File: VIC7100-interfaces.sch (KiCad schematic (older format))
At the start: 56 parts, among them Q5 DMG1012UW, U13 VIC7100

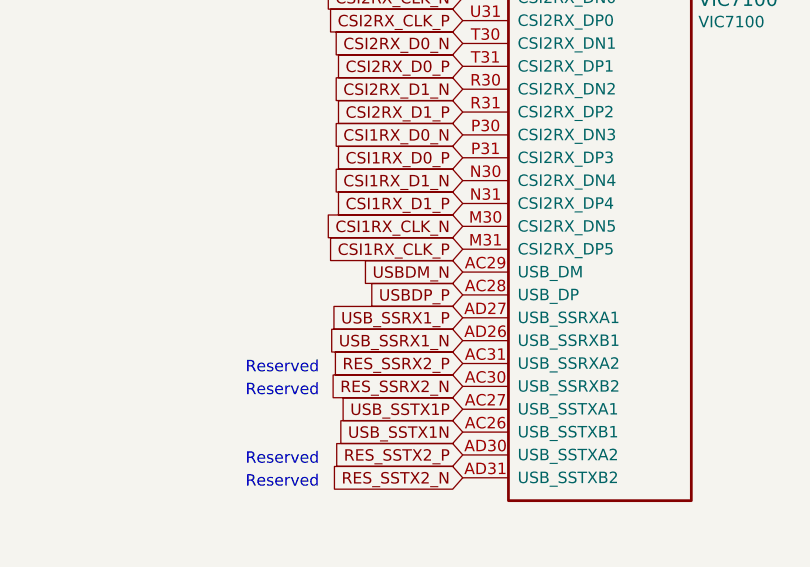
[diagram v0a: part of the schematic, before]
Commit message: Routed USB, QSPI, JTAG
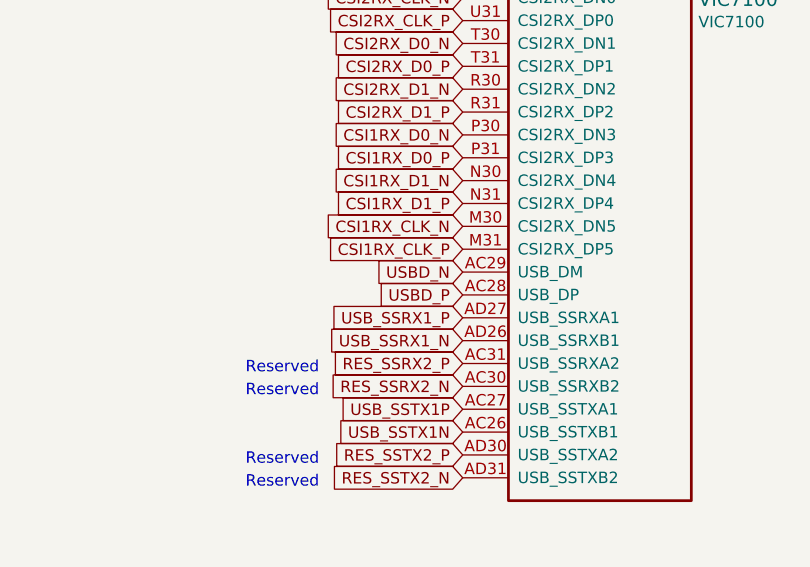
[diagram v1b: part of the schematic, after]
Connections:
- net USBDM_N renamed USBD_N
- net USBDP_P renamed USBD_P
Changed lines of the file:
@@
 CSI1RX_CLK_P
 Text GLabel 8975 4650 0    50   Input ~ 0
-USBDM_N
+USBD_N
 Text GLabel 8975 4750 0    50   Input ~ 0
-USBDP_P
+USBD_P
 Text GLabel 11925 2525 1    50   Input ~ 0
 VCC_3V3

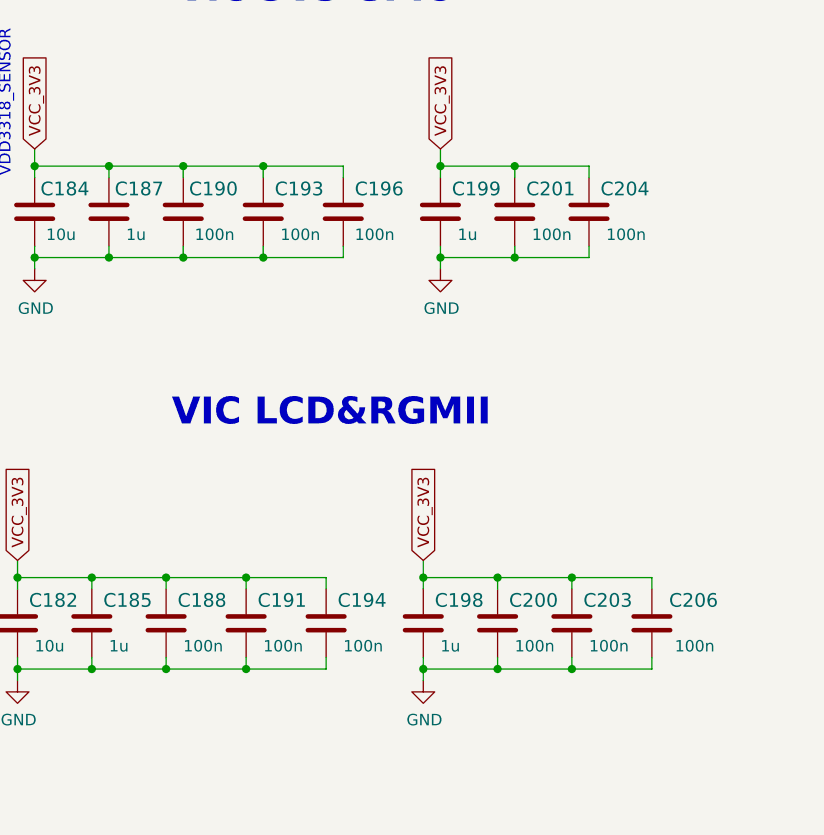
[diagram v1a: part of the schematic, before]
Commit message: Caps cleared, module connnetors' GND optimized
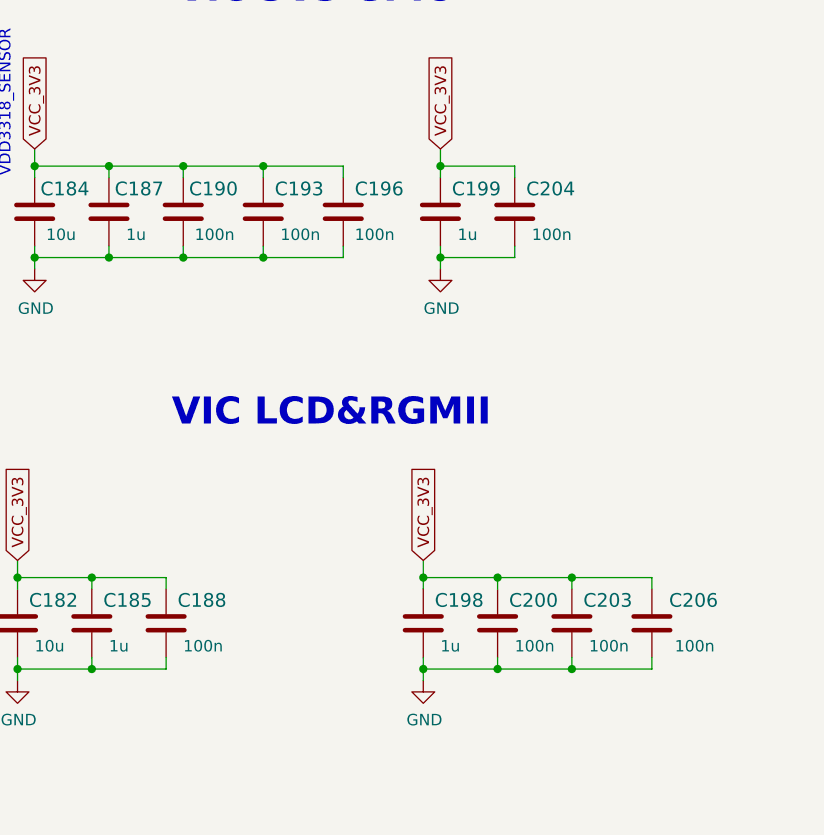
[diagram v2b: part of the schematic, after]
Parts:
- removed C191, C194, C201: C_100n_0201, arvsom-footprints:0201-res, symbol arvsom:C_100n_0201
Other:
- moved on the sheet: C204
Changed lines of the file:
@@
 Wire Wire Line
 	14025 2650 14025 2600
-Connection ~ 14025 2600
-Wire Wire Line
-	14025 2600 14350 2600
-Wire Wire Line
-	14350 2650 14350 2600
 Wire Wire Line
 	14025 2950 14025 3000
-Connection ~ 14025 3000
-Wire Wire Line
-	14025 3000 14350 3000
-Wire Wire Line
-	14350 2950 14350 3000
 $Comp
 L arvsom:C_1u_0402 C?
@@
 $Comp
 L arvsom:C_100n_0201 C?
-U 1 1 60E65122
+U 1 1 60E6512B
 P 14025 2800
-AR Path="/607683D6/60E65122" Ref="C?"  Part="1"
-AR Path="/60805CEC/60E65122" Ref="C201"  Part="1"
-F 0 "C201" H 14075 2900 60  0000 L CNN
+AR Path="/607683D6/60E6512B" Ref="C?"  Part="1"
+AR Path="/60805CEC/60E6512B" Ref="C204"  Part="1"
+F 0 "C204" H 14075 2900 60  0000 L CNN
 F 1 "C_100n_0201" H 14025 2650 60  0001 C CNN
 F 2 "arvsom-footprints:0201-res" H 14225 3000 60  0001 L CNN
@@
 F 6 "100n" H 14100 2700 50  0000 L CNN "Val"
 	1    14025 2800
-	1    0    0    -1
-$EndComp
-$Comp
-L arvsom:C_100n_0201 C?
-U 1 1 60E6512B
-P 14350 2800
-AR Path="/607683D6/60E6512B" Ref="C?"  Part="1"
-AR Path="/60805CEC/60E6512B" Ref="C204"  Part="1"
-F 0 "C204" H 14400 2900 60  0000 L CNN
-F 1 "C_100n_0201" H 14350 2650 60  0001 C CNN
-F 2 "arvsom-footprints:0201-res" H 14550 3000 60  0001 L CNN
-F 3 "" H 14350 2800 50  0001 C CNN
-F 4 "YAGEO" H 14550 3200 60  0001 L CNN "Manufacturer"
-F 5 "CC0201KRX6S5BB104" H 14550 3100 60  0001 L CNN "MPN"
-F 6 "100n" H 14425 2700 50  0000 L CNN "Val"
-	1    14350 2800
 	1    0    0    -1
 $EndComp
@@
 Wire Wire Line
 	12500 4450 12500 4400
-Connection ~ 12500 4400
 Wire Wire Line
 	12175 4750 12175 4800
@@
 Wire Wire Line
 	12500 4750 12500 4800
-Connection ~ 12500 4800
 $Comp
 L arvsom:C_10u_0402 C?
@@
 	1    0    0    -1
 $EndComp
-$Comp
-L arvsom:C_100n_0201 C?
-U 1 1 60E65169
-P 12850 4600
-AR Path="/607683D6/60E65169" Ref="C?"  Part="1"
-AR Path="/60805CEC/60E65169" Ref="C191"  Part="1"
-F 0 "C191" H 12900 4700 60  0000 L CNN
-F 1 "C_100n_0201" H 12850 4450 60  0001 C CNN
-F 2 "arvsom-footprints:0201-res" H 13050 4800 60  0001 L CNN
-F 3 "" H 12850 4600 50  0001 C CNN
-F 4 "YAGEO" H 13050 5000 60  0001 L CNN "Manufacturer"
-F 5 "CC0201KRX6S5BB104" H 13050 4900 60  0001 L CNN "MPN"
-F 6 "100n" H 12925 4500 50  0000 L CNN "Val"
-	1    12850 4600
-	1    0    0    -1
-$EndComp
-Wire Wire Line
-	13200 4750 13200 4800
-Wire Wire Line
-	13200 4450 13200 4400
-$Comp
-L arvsom:C_100n_0201 C?
-U 1 1 60E65174
-P 13200 4600
-AR Path="/607683D6/60E65174" Ref="C?"  Part="1"
-AR Path="/60805CEC/60E65174" Ref="C194"  Part="1"
-F 0 "C194" H 13250 4700 60  0000 L CNN
-F 1 "C_100n_0201" H 13200 4450 60  0001 C CNN
-F 2 "arvsom-footprints:0201-res" H 13400 4800 60  0001 L CNN
-F 3 "" H 13200 4600 50  0001 C CNN
-F 4 "YAGEO" H 13400 5000 60  0001 L CNN "Manufacturer"
-F 5 "CC0201KRX6S5BB104" H 13400 4900 60  0001 L CNN "MPN"
-F 6 "100n" H 13275 4500 50  0000 L CNN "Val"
-	1    13200 4600
-	1    0    0    -1
-$EndComp
-Wire Wire Line
-	12500 4400 12850 4400
-Wire Wire Line
-	12500 4800 12850 4800
-Wire Wire Line
-	12850 4450 12850 4400
-Connection ~ 12850 4400
-Wire Wire Line
-	12850 4400 13200 4400
-Wire Wire Line
-	12850 4750 12850 4800
-Connection ~ 12850 4800
-Wire Wire Line
-	12850 4800 13200 4800
 Text GLabel 13625 4325 1    50   Input ~ 0
 VCC_3V3
